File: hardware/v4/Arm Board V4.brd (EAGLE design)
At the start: 152.4 x 50.8 mm, 35 parts, among them IC1 4503D, IC2 4503D, IC7 7812DT, IC9 7812DT, Q3 Q_LTC490, U2 XBEE-1B3

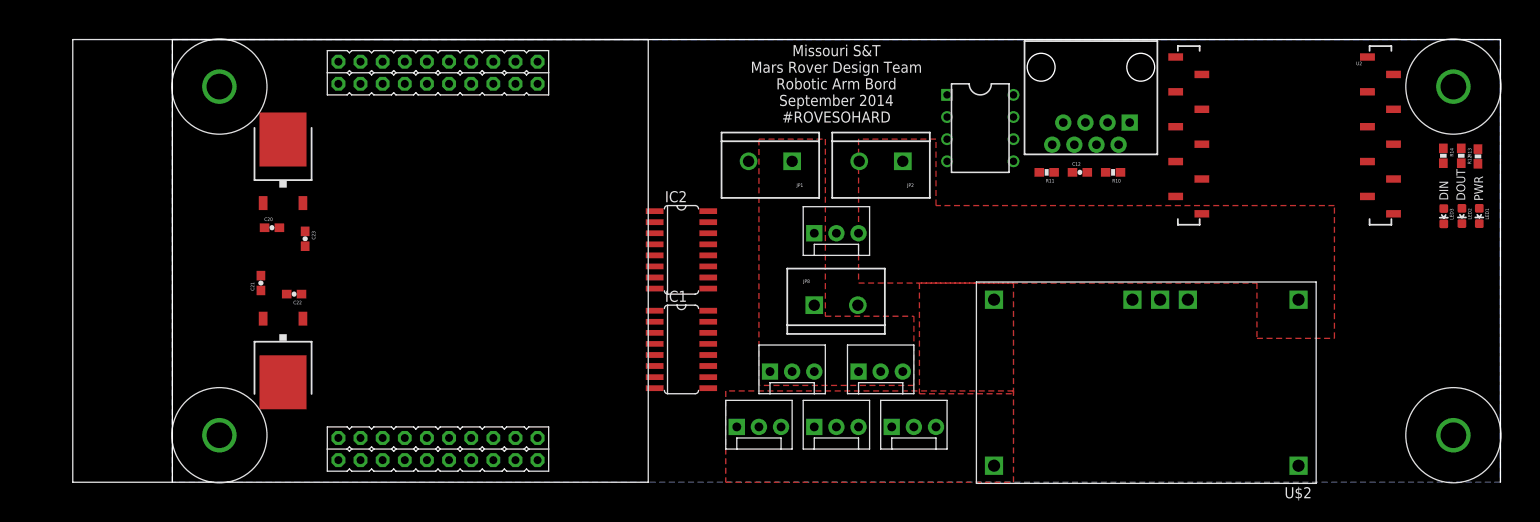
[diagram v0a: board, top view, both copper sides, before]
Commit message: Continued work on V4
Started to route power and fixed inconsistency
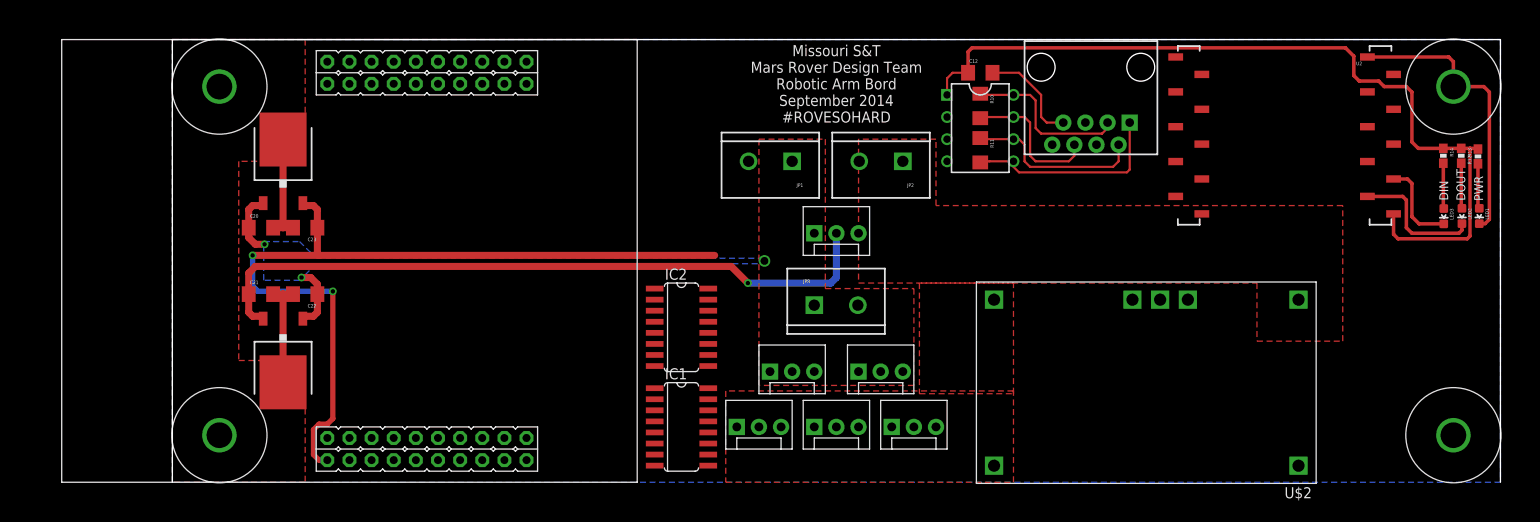
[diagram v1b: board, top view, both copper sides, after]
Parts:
- C12: device SparkFun-Capacitors:0603-CAP -> SparkFun-Capacitors:1206
- C20, C21, C22, C23: value 0.1uF -> .1uF; device SparkFun-Capacitors:0603-CAP -> SparkFun-Capacitors:1206
- R10, R11: device SparkFun-Passives:0603-RES -> SparkFun-Passives:1206
- moved R10 17.0 mm to (92.7, 43.2), turned to 270 degrees
- moved C12 16.2 mm to (92.7, 47.0)
- moved IC1 8.89 mm to (58.4, 6.35)
- moved IC2 8.89 mm to (58.4, 17.8)
- moved R11 8.03 mm to (92.7, 38.1), turned to 270 degrees
- moved C20 1.27 mm to (10.2, 29.2)
- moved C21 1.27 mm to (10.2, 21.6), turned to 0 degrees
- moved C22 1.27 mm to (15.2, 21.6)
- moved C23 1.27 mm to (15.2, 29.2), turned to 180 degrees
- moved U$1 1.27 mm to (-12.7, 0.00)
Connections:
- net EN_A_1 renamed TX_7
- net IN1_A_2 renamed RX_7
- net RESET renamed RST
- net RXD5 renamed RX_5
- net TXD5 renamed TX_5
- removed net A0: U$1.PE3
- removed net A10: U$1.PB4
- removed net A11: U$1.PB5
- removed net A7: U$1.PD0
- removed net EN485: U$1.PB3
- removed net EN_A_2: U$1.PB7
- removed net EN_A_3: U$1.PB6
- removed net EN_B_1: U$1.PE2
- removed net EN_B_2: U$1.PB2
- removed net IN1_A_1: U$1.PD1
- removed net IN1_A_3: U$1.PA3
- removed net IN1_B_1: U$1.PD2
- removed net IN1_B_2: U$1.PF2
- removed net IN2_A_1: U$1.PA2
- removed net IN2_A_2: U$1.PF0
- removed net IN2_A_3: U$1.PA4
- removed net IN2_B_1: U$1.PD3
- removed net IN2_B_2: U$1.PF3
- removed net RXD1: Q3.2, U$1.PC6
- removed net RXD2: U$1.PC4
- removed net TXD1: Q3.3, U$1.PC7
- removed net TXD2: U$1.PC5
- new net RX_1: Q3.2, U$1.PC4
- new net RX_2: U$1.PD6
- new net RX_3: U$1.PC6
- new net TX_1: Q3.3, U$1.PC5
- new net TX_2: U$1.PD7
- new net TX_3: U$1.PC7
- new net VBUS: U$1.VBUS
- net +5V: no longer U$1.VBUS
- net RXD3: no longer U$1.PD6
- net TXD3: no longer U$1.PD7
- net XRESET: no longer U$1.PF4
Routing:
- net +3V3: track 0.00 -> 192.0 mm, vias 0 -> 2
- net +5V: track 0.00 -> 80.4 mm, vias 0 -> 1
- net GND: track 0.00 -> 70.1 mm
- net N$5: track 0.00 -> 23.6 mm
- net N$1: track 0.00 -> 20.5 mm
- net N$3: track 0.00 -> 19.2 mm
- net N$2: track 0.00 -> 16.7 mm
- net RXD3: track 0.00 -> 15.4 mm
- net +12V: track 0.00 -> 14.7 mm, vias 0 -> 3
- net TXD3: track 0.00 -> 10.1 mm
- net N$6: track 0.00 -> 5.23 mm
- net N$4: track 0.00 -> 5.21 mm
- net N$38: track 0.00 -> 5.17 mm
- added copper zone on layer 16, net +12V
- added copper zone on layer 1, net GND

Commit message: Router power and data lines and assigned pins
Started to route more of the data lines to where they will go.  As well
as working on assigning pins to components.
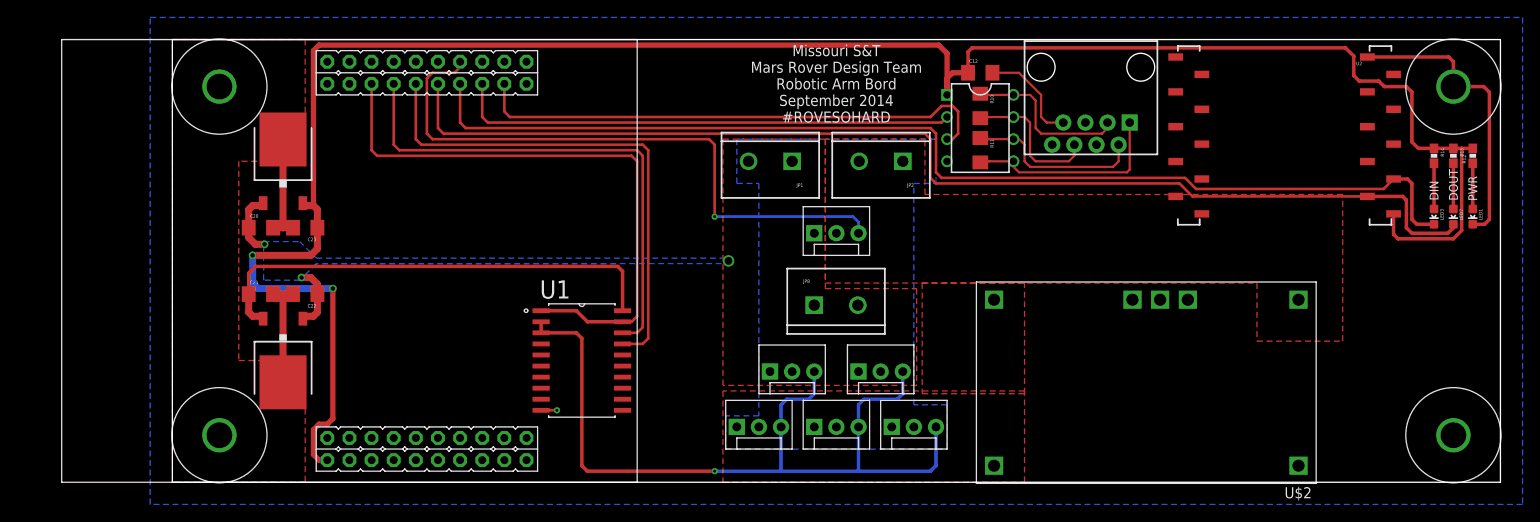
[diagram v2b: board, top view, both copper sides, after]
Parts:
- removed IC1, IC2: 4503D, 45xx:SO16
- added U1: SN74LS241DW, 74LS241:SOIC127P1030X265-20N
- moved LED3 1.12 mm to (144.8, 30.5)
- moved R14 1.07 mm to (144.8, 37.5)
- moved LED2 0.98 mm to (147.0, 30.5)
- moved R13 0.90 mm to (147.0, 37.5)
- moved LED1 0.75 mm to (149.2, 30.5)
- moved R12 0.60 mm to (149.2, 37.5)
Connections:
- removed net RXD3: LED2.C, U2.2
- removed net TXD3: LED3.C, U2.3
- removed net VDD: IC1.16, IC2.16
- removed net VSS: IC1.8, IC2.8
- new net 5VIN: JP7.2
- new net DC_1: U$1.PB3, U1.1, U1.19
- new net DDATA_1: JP10.3, JP11.3, JP12.3, JP13.3, JP9.3, U1.2, U1.3
- net +5V: now also U1.20; no longer JP7.2
- net GND: now also U1.10
- net LA_PWM: now also U$1.PB6
- net RX_1: now also U1.18; no longer Q3.2
- net RX_2: now also Q3.2
- net RX_3: now also LED2.C, U2.2
- net TX_1: now also U1.17; no longer Q3.3
- net TX_2: now also Q3.3
- net TX_3: now also LED3.C, U2.3
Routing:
- net RX_3: track 0.00 -> 131.7 mm
- net TX_3: track 0.00 -> 127.0 mm
- net DDATA_1: track 0.00 -> 96.7 mm, vias 0 -> 1
- net LA_PWM: track 0.00 -> 71.2 mm, vias 0 -> 1
- net DC_1: track 0.00 -> 68.2 mm
- net TX_2: track 0.00 -> 60.4 mm
- net RX_1: track 0.00 -> 58.3 mm
- net TX_1: track 0.00 -> 58.3 mm
- net RX_2: track 0.00 -> 57.7 mm
- net +3V3: track 192.0 -> 239.9 mm
- net +5V: track 80.4 -> 54.4 mm, vias 1 -> 0
- net RXD3: track 15.4 -> 0.00 mm
- net TXD3: track 10.1 -> 0.00 mm
- net GND: track 70.1 -> 72.7 mm, vias 0 -> 1

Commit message: mn vc,m
nbmnb m
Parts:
- moved U1 1.91 mm to (45.1, 14.0)
- moved LED1 1.27 mm to (149.2, 31.8)
- moved LED2 1.27 mm to (147.0, 31.8)
- moved LED3 1.27 mm to (144.8, 31.8)
- moved U2 0.32 mm to (127.6, 51.1)
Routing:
- net +12V: track 14.7 -> 19.3 mm
- net +3V3: track 239.9 -> 237.8 mm
- net TX_1: track 58.3 -> 56.4 mm
- net RX_1: track 58.3 -> 56.4 mm
- net DDATA_1: track 96.7 -> 98.6 mm
- net DC_1: track 68.2 -> 66.3 mm
- net N$38: track 5.49 -> 3.99 mm
- net +5V: track 54.4 -> 55.9 mm
- net TX_3: track 127.0 -> 125.7 mm
- net N$6: track 5.26 -> 3.99 mm
- net N$4: track 5.26 -> 3.99 mm
- net RX_3: track 131.7 -> 130.6 mm
- net GND: track 72.7 -> 71.7 mm

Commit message: Added a few things and cleaned up some stuff
Added a few things from last night but mostly cleaning up traces and
adding parts to it.  Commit message last night was by Seto so ignore the
message.
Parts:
- added JP4, JP5: (no value), SparkFun-Connectors:1X04_NO_SILK
- added Q1, Q2, Q4: MOSFET-NCHANNELFQP30N06L, SparkFun-DiscreteSemi:TO220V
- added R3, R6, R7: 150, SparkFun-Passives:1206
- moved U1 10.2 mm to (55.2, 14.0)
- moved U$1 7.62 mm to (-5.08, 0.00)
- moved Q3 4.45 mm to (92.7, 45.1)
- moved C12 1.91 mm to (92.7, 48.9), flipped to the bottom, turned to 180 degrees
- moved R10 1.91 mm to (92.7, 45.1), flipped to the bottom
- moved R11 1.91 mm to (92.7, 40.0), flipped to the bottom
- moved JP2 1.80 mm to (85.1, 38.1)
- moved JP1 1.80 mm to (72.4, 38.1)
- moved U$3 0.32 mm to (105.4, 47.9)
- moved U2 0.32 mm to (128.0, 51.1)
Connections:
- new net O1: JP4.2, JP5.2, Q1.2
- new net O2: JP4.3, JP5.3, Q2.2
- new net O3: JP4.4, JP5.4, Q4.2
- new net PWM1: Q1.1, R3.2, U$1.PD1
- new net PWM2: Q2.1, R6.2, U$1.PD2
- new net PWM3: Q4.1, R7.2, U$1.PD3
- net +12V: now also JP4.1, JP5.1
- net GND: now also Q1.3, Q2.3, Q4.3, R3.1, R6.1, R7.1
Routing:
- net PWM3: track 0.00 -> 165.2 mm, vias 0 -> 2
- net PWM2: track 0.00 -> 163.1 mm, vias 0 -> 2
- net PWM1: track 0.00 -> 161.7 mm, vias 0 -> 2
- net +12V: track 19.3 -> 111.2 mm, vias 3 -> 4
- net O3: track 0.00 -> 14.2 mm
- net O1: track 0.00 -> 13.6 mm
- net O2: track 0.00 -> 12.0 mm
- net DDATA_1: track 98.6 -> 89.1 mm
- net RX_2: track 57.7 -> 49.0 mm
- net TX_2: track 60.4 -> 52.1 mm
- net +5V: track 55.9 -> 63.8 mm
- net LA_PWM: track 71.2 -> 63.5 mm
- net TX_3: track 125.7 -> 119.2 mm
- net RX_3: track 130.6 -> 125.7 mm
- net N$5: track 23.6 -> 27.2 mm
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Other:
- board text added: "+"
- board text added: "-"
- board text added: "12V"
- board text added: "30V"
- board text added: "AX-12"
- board text added: "Linear Servo"
- board text added: "MX-64"
- board text added: "Missouri S&T Mars Rover Design Team Robotic Arm Bord November 2014 #ROVESOHARD"
- board text removed: "Missouri S&T Mars Rover Design Team Robotic Arm Bord September 2014 #ROVESOHARD"

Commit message: A lot of updates getting close to a final board
Did a lot of changes that got the board closer to the final version.
Skipped a lot of commits because who cares and github was not getting
along with me.
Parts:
- removed C20, C21, C22, C23: .1uF, SparkFun-Capacitors:1206
- removed IC7, IC9: 7812DT, linear:TO252
- removed JP1, JP2: M025MM, SparkFun-Connectors:SCREWTERMINAL-5MM-2
- removed JP13: (no value), SparkFun-Connectors:MOLEX-1X3
- removed JP5: (no value), SparkFun-Connectors:1X04_NO_SILK
- removed Q1, Q2, Q4: MOSFET-NCHANNELFQP30N06L, SparkFun-DiscreteSemi:TO220V
- removed Q3: Q_LTC490, PCB0M1:DIP8
- added C1: .1uF, SparkFun-Capacitors:1206
- added C3: (no value), SparkFun-Passives:PANASONIC_C
- added C5: .22uF, SparkFun-Capacitors:1206
- added C6: 4.7uF, SparkFun-Capacitors:1206
- added C7: 1uF, SparkFun-Capacitors:1206
- added C8: 10uF, SparkFun-Capacitors:EIA3216
- added IC2: REG1118, burr-brown:SOT223
- added JP3: M025MM, SparkFun-Connectors:SCREWTERMINAL-5MM-2
- added LED5: RED, SparkFun-LED:LED-0603
- added R1: 16.5k, SparkFun-Passives:1206
- added R2, R4, R5: 10k, SparkFun-Resistors:1206
- added R9: 1k, SparkFun-Passives:1206
- added U$4: MAX3077, MAX3077:MAX3070E
- added U3: LSM9DS0, SparkFun-DigitalIC:LGA-24
- JP4: device SparkFun-Connectors:1X04_NO_SILK -> SparkFun-Connectors:SCREWTERMINAL-3.5MM-4
- LED1, LED2: value Red -> RED
- LED3: value Green -> GREEN
- R12, R13, R14: device SparkFun-Resistors:0603-RES -> SparkFun-Passives:1206
- R3, R6, R7: value 150 -> 10k; device SparkFun-Passives:1206 -> SparkFun-Resistors:1206
- moved JP4 78.9 mm to (68.6, 33.0), turned to 180 degrees
- moved H3 27.7 mm to (119.4, 47.0)
- moved H4 27.7 mm to (119.4, 3.81)
- moved R14 27.5 mm to (119.4, 26.9)
- moved LED3 27.4 mm to (119.4, 21.6)
- moved R13 27.2 mm to (121.9, 26.9)
- moved LED2 27.1 mm to (121.9, 21.6)
- moved R12 26.9 mm to (124.5, 26.9)
- moved LED1 26.8 mm to (124.5, 21.6)
- moved JP7 23.3 mm to (55.6, 14.0)
- moved JP8 19.4 mm to (54.6, 23.8)
- moved C12 16.8 mm to (75.9, 48.3), flipped to the top, turned to 0 degrees
- moved U$2 16.5 mm to (95.2, 11.4)
- moved U2 14.9 mm to (113.0, 51.1)
- moved JP11 13.7 mm to (68.9, 6.35)
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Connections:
- removed net 5VIN: JP7.2
- removed net O1: JP4.2, JP5.2, Q1.2
- removed net O2: JP4.3, JP5.3, Q2.2
- removed net O3: JP4.4, JP5.4, Q4.2
- removed net VBUS: U$1.VBUS
- new net +3.3V: IC2.1, R12.2, R13.1, R14.1, U2.1
- new net CS_G: R4.1, U3.19
- new net CS_XM: R5.1, U3.20
- new net DEN_G: U3.10
- new net DRDY_G: U3.12
- new net INT1_XM: U3.13
- new net INT2_XM: U3.14
- new net INT_G: U3.11
- new net N$10: C5.1, U3.9
- new net N$11: C5.2, U3.8
- new net N$12: C6.1, U3.7
- new net N$14: LED5.A, R9.1
- new net N$9: R1.2, U$2.4
- new net SCL: R3.1, U$1.PA6, U3.21
- new net SDA: R2.1, U$1.PA7, U3.24
- new net SDO_G: R7.1, U3.22
- new net SDO_XM: R6.1, U3.23
- net +12V: now also JP3.1, JP4.3; no longer C20.1, C22.1, IC7.1, IC9.1, JP1.1, JP13.2, JP4.1, JP5.1
- net +3V3: now also C7.1, C8.A, R2.2, R3.2, R4.2, R5.2, R6.2, R7.2, U3.15, U3.16, U3.17, U3.18; no longer C12.1, C23.1, IC9.2, Q3.1, R12.2, R13.1, R14.1, U2.1
- net +5V: now also C12.1, IC2.3, JP4.4, JP7.2, U$1.VBUS, U$4.VCC; no longer C21.1, IC7.2
- net 14.8V: now also C3.+
- net DDATA_1: no longer JP13.3
- net GND: now also C1.2, C3.-, C6.2, C7.2, C8.C, IC2.2, JP3.2, JP4.1, LED5.C, R1.1, U$4.GND, U3.2, U3.3, U3.4, U3.5, U3.6; no longer C20.2, C21.2, C22.2, C23.2, IC7.3, IC9.3, JP1.2, JP13.1, JP2.2, Q1.3, Q2.3, Q3.4, Q4.3, R3.1, R6.1, R7.1
- net N$1: now also U$4.Z; no longer Q3.6
- net N$2: now also U$4.B; no longer Q3.7
- net N$3: now also U$4.A; no longer Q3.8
- net N$5: now also U$4.Y; no longer Q3.5
- net PWM1: no longer Q1.1, R3.2
- net PWM2: no longer Q2.1, R6.2
- net PWM3: no longer Q4.1, R7.2
- net RX_2: now also U$4.RO; no longer Q3.2
- net TX_2: now also U$4.DI; no longer Q3.3
- net VIN: now also C1.1, JP4.2, R9.2; no longer JP2.1
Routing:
- net +3V3: track 236.5 -> 45.0 mm, vias 2 -> 0
- net PWM3: track 165.2 -> 0.00 mm, vias 2 -> 0
- net PWM2: track 163.1 -> 0.00 mm, vias 2 -> 0
- net PWM1: track 161.7 -> 0.00 mm, vias 2 -> 0
- net +5V: track 63.8 -> 181.4 mm, vias 0 -> 4
- net +12V: track 111.2 -> 0.00 mm, vias 4 -> 0
- net N$14: track 0.00 -> 89.0 mm
- net GND: track 73.5 -> 14.6 mm, vias 1 -> 9
- net +3.3V: track 0.00 -> 35.4 mm, vias 0 -> 2
- net SCL: track 0.00 -> 26.8 mm
- net SDA: track 0.00 -> 20.5 mm
- net VIN: track 0.00 -> 18.5 mm
- net TX_3: track 119.2 -> 134.2 mm
- net O3: track 14.2 -> 0.00 mm
- net O1: track 13.6 -> 0.00 mm
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- removed copper zone on layer 16, net +12V
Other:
- board size 152.4 x 50.8 mm -> 127 x 50.8 mm
- board text added: "5V"
- board text added: "GND"
- board text added: "Missouri S&T Mars Rover Design Team Robotic Arm Bord November 2014 Eric Mullis #ROVESOHARD"
- board text added: "PWM"
- board text added: "X"
- board text added: "Y"
- board text added: "Z"
- board text removed: "30V"
- board text removed: "Missouri S&T Mars Rover Design Team Robotic Arm Bord November 2014 #ROVESOHARD"

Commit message: No significant changes
No significant changes
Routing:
- net +5V: track 181.4 -> 182.5 mm
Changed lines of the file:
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@@
 <wire x1="58.08" y1="33.02" x2="47.8155" y2="33.02" width="0.6096" layer="16"/>
 <via x="47.8155" y="33.02" extent="1-16" drill="0.5"/>
-<wire x1="47.8155" y1="33.02" x2="47.8155" y2="19.1389" width="0.6096" layer="1"/>
+<wire x1="47.8155" y1="33.02" x2="47.8155" y2="19.812" width="0.6096" layer="1"/>
+<wire x1="47.8155" y1="19.812" x2="47.8155" y2="19.1389" width="0.6096" layer="1"/>
 <wire x1="47.8155" y1="19.1389" x2="47.2186" y2="19.05" width="0.4064" layer="1"/>
 <via x="46.6725" y="19.05" extent="1-16" drill="0.5"/>
@@
 <wire x1="57.785" y1="12.065" x2="58.1025" y2="12.3825" width="0.4064" layer="1"/>
 <wire x1="58.1025" y1="12.3825" x2="58.1025" y2="13.97" width="0.4064" layer="1"/>
-<wire x1="46.6725" y1="19.05" x2="45.72" y2="19.05" width="0.4572" layer="1"/>
-<wire x1="45.72" y1="19.05" x2="45.4025" y2="19.3675" width="0.4572" layer="1"/>
-<wire x1="45.4025" y1="19.3675" x2="45.4025" y2="24.4475" width="0.4572" layer="1"/>
-<wire x1="45.4025" y1="24.4475" x2="44.7675" y2="25.0825" width="0.4572" layer="1"/>
-<wire x1="44.7675" y1="25.0825" x2="13.335" y2="25.0825" width="0.4572" layer="1"/>
-<wire x1="13.335" y1="25.0825" x2="12.7" y2="24.4475" width="0.4572" layer="1"/>
-<wire x1="12.7" y1="24.4475" x2="12.7" y2="5.08" width="0.4572" layer="1"/>
 <wire x1="94.615" y1="49.53" x2="93.98" y2="50.165" width="0.4572" layer="1"/>
 <wire x1="74.4825" y1="48.26" x2="74.4825" y2="49.7175" width="0.4572" layer="1"/>
@@
 <wire x1="111.5314" y1="43.9166" x2="110.998" y2="44.45" width="0.4572" layer="1"/>
 <wire x1="110.998" y1="44.45" x2="102.362" y2="44.45" width="0.4572" layer="1"/>
+<wire x1="12.7" y1="5.08" x2="11.938" y2="5.08" width="0.6096" layer="1"/>
+<wire x1="11.938" y1="5.08" x2="11.43" y2="4.572" width="0.6096" layer="1"/>
+<wire x1="11.43" y1="4.572" x2="11.43" y2="1.778" width="0.6096" layer="1"/>
+<wire x1="11.43" y1="1.778" x2="11.938" y2="1.27" width="0.6096" layer="1"/>
+<wire x1="11.938" y1="1.27" x2="36.576" y2="1.27" width="0.6096" layer="1"/>
+<wire x1="36.576" y1="1.27" x2="37.084" y2="1.778" width="0.6096" layer="1"/>
+<wire x1="37.084" y1="1.778" x2="37.084" y2="5.588" width="0.6096" layer="1"/>
+<wire x1="37.084" y1="5.588" x2="36.322" y2="6.35" width="0.6096" layer="1"/>
+<wire x1="36.322" y1="6.35" x2="36.322" y2="19.558" width="0.6096" layer="1"/>
+<wire x1="36.322" y1="19.558" x2="36.83" y2="20.066" width="0.6096" layer="1"/>
+<wire x1="36.83" y1="20.066" x2="47.5615" y2="20.066" width="0.6096" layer="1"/>
+<wire x1="47.5615" y1="20.066" x2="47.8155" y2="19.812" width="0.6096" layer="1"/>
 </signal>
 <signal name="+12V">
